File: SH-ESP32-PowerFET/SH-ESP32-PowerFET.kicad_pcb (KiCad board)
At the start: 4 copper layers, 83 x 55.5 mm, 75 parts, among them J101 DBT50G-9.5-4P, J102 DBT50G-9.5-2P, J103 GPIO, J104 Qwiic, J105 MPDI, J106 Conn_01x04, J301 VIN_GND1, Q301 IRF5210STRLPBF, Q302 IRF5210STRLPBF, Q303 IRF5210STRLPBF, Q304 IRF5210STRLPBF, U101 ATtiny1614-SSNR, U301 EL3H7(C)(TA)-G, U302 EL3H7(C)(TA)-G, U303 EL3H7(C)(TA)-G, U304 INA226AIDGSR, U305 INA226AIDGSR, U306 INA226AIDGSR, U307 EL3H7(C)(TA)-G, U308 INA226AIDGSR, U701 RCLAMP0524P-N

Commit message: Updated Shunt Part number
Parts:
- R315: value 0.002ohm /3W -> 0.002ohm/3W

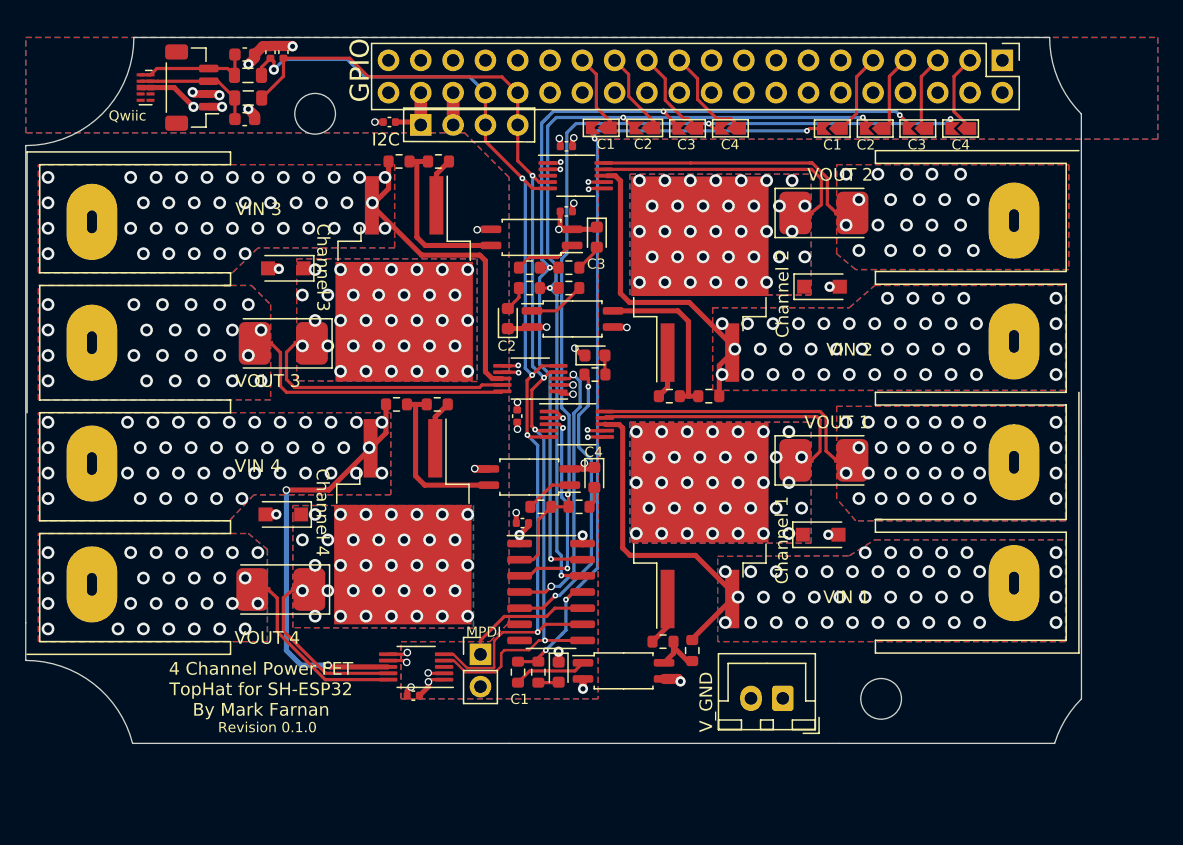
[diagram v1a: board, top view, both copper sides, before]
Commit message: Major Refactor - Based on new requirments from Karl and feedback. - Made from latest blank with more PCB area, and new interconnect positions for I2C,  GPIO etc - Removed opto couplers - I2C now isolated at board input - Provision for Switched inputs and LED outputs - PSU onboard. - I2C only, removed reliance on GPIO header - Can be used as SH-ESP32 HAT,  or as standalone / daisy chained board on DIN rail etc.
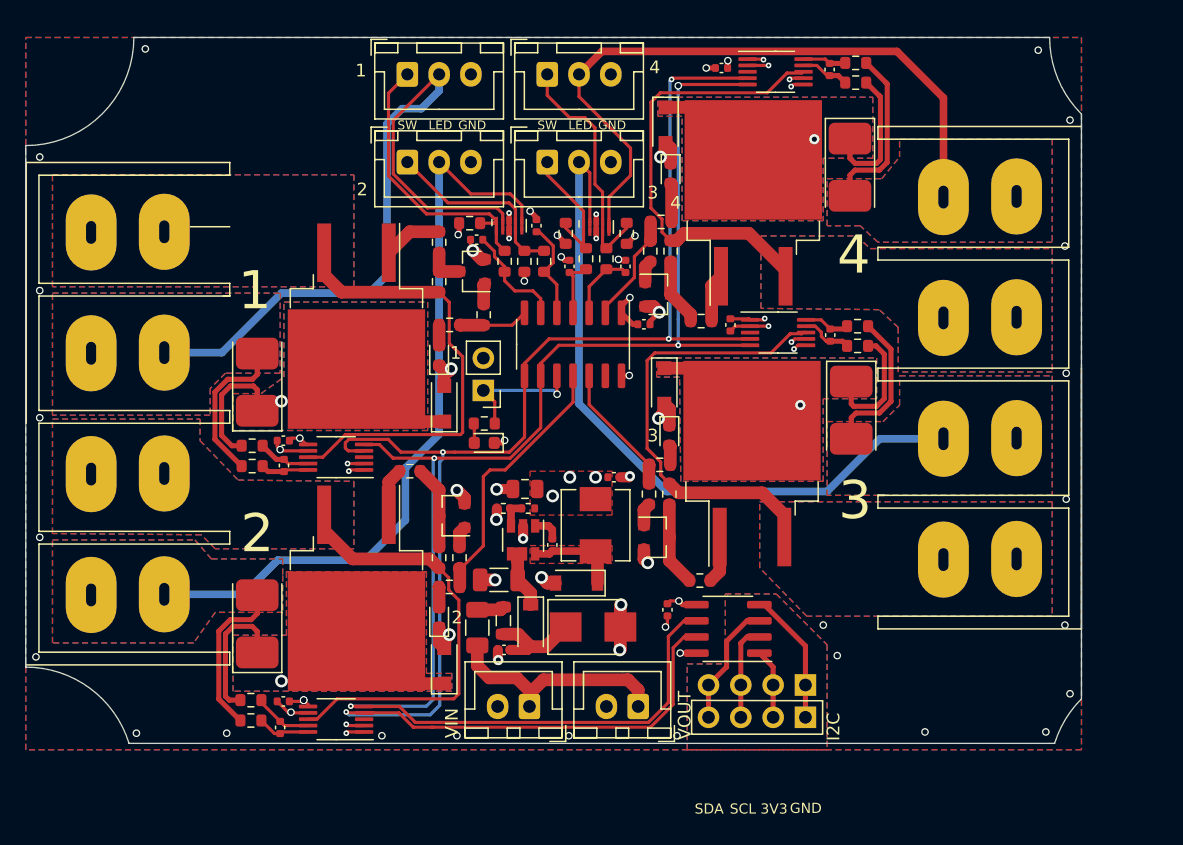
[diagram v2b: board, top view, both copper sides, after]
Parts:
- removed C105, C106: 33pF, Capacitor_SMD:C_0402_1005Metric
- removed D303, D307: BLUE LED, LED_SMD:LED_0603_1608Metric
- removed D304, D305, D306, D308: SM4007PL, Diode_SMD:D_SOD-123F
- removed FB102, FB103: GZ2012D101TF, Inductor_SMD:L_0805_2012Metric
- removed J103: GPIO, Connector_PinHeader_2.54mm:PinHeader_2x20_P2.54mm_Vertical
- removed J104: Qwiic, Connector_JST:JST_SH_BM04B-SRSS-TB_1x04-1MP_P1.00mm_Vertical
- removed J301: VIN_GND1, Connector_JST:JST_XH_B2B-XH-A_1x02_P2.50mm_Vertical
- removed JP101, JP102, JP103, JP104, JP105, JP106, JP107, JP108: Solder Jumper, yacht_hardware:SolderJumper-2_P1.3mm_Open_TrianglePad_Narrow
- removed LOGO_CC: LOGO, SH-ESP32:cc-by-sa_silkscreen
- removed OSHW: OSHW-Logo2_14.6x12mm_SilkScreen, Symbol:OSHW-Logo2_14.6x12mm_SilkScreen
- removed Q303, Q304: IRF5210STRLPBF, Package_TO_SOT_SMD:TO-263-2
- removed R308, R309, R318: 10k, Resistor_SMD:R_0603_1608Metric
- removed R310, R311, R312, R319: 1k, Resistor_SMD:R_0603_1608Metric
- removed R313, R314, R315, R320: 0.002ohm/3W, yacht_hardware:D_2512_Shunt
- removed R316: 2k, Resistor_SMD:R_0603_1608Metric
- removed R317: 220R, Resistor_SMD:R_0603_1608Metric
- removed U302, U303, U307: EL3H7(C)(TA)-G, Package_SO:SOP-4_4.4x2.6mm_P1.27mm
- removed U304, U305, U306, U308: INA226AIDGSR, Package_SO:VSSOP-10_3x3mm_P0.5mm
- added C101: 1nf, Capacitor_SMD:C_0402_1005Metric, F.Cu at (124.5, 72.9)
- added C104: 1nf, Capacitor_SMD:C_0402_1005Metric, F.Cu at (136.2, 75.0)
- added C301: 100nF, Capacitor_SMD:C_0402_1005Metric, F.Cu at (109.3, 90.7)
- added C401: 100nF, Capacitor_SMD:C_0402_1005Metric, F.Cu at (109.0, 111.2)
- added C501: 100nF, Capacitor_SMD:C_0402_1005Metric, F.Cu at (152.2, 80.4)
- added C601: 100nF, Capacitor_SMD:C_0402_1005Metric, F.Cu at (152.2, 59.5)
- added C701: 10uF/50V, Capacitor_SMD:C_1206_3216Metric, F.Cu at (126.2, 99.7)
- added C702: 10nF/50V, Capacitor_SMD:C_0402_1005Metric, F.Cu at (126.6, 105.2)
- added C703: 100nF, Capacitor_SMD:C_0402_1005Metric, F.Cu at (130.4, 96.9)
- added C704: 22uF/6.3V, Capacitor_SMD:C_0805_2012Metric, F.Cu at (128.2, 92.5)
- added C705: 10nF/50V, Capacitor_SMD:C_0402_1005Metric, F.Cu at (135.2, 91.6)
- added D401: BLUE LED, LED_SMD:LED_0603_1608Metric, F.Cu at (121.5, 102.6)
- added D402: SM4007PL, Diode_SMD:D_SOD-123F, F.Cu at (121.9, 106.4)
- added D501: BLUE LED, LED_SMD:LED_0603_1608Metric, F.Cu at (139.6, 88.3)
- added D502: SM4007PL, Diode_SMD:D_SOD-123F, F.Cu at (139.2, 84.4)
- added D601: BLUE LED, LED_SMD:LED_0603_1608Metric, F.Cu at (139.7, 67.7)
- added D602: SM4007PL, Diode_SMD:D_SOD-123F, F.Cu at (139.3, 63.9)
- added D701: SMBJ33CA, Diode_SMD:D_SMB, F.Cu at (133.6, 103.3)
- added D702: B5819W, Diode_SMD:D_SOD-123, F.Cu at (132.3, 99.9)
- added D703: B5819W, Diode_SMD:D_SOD-123, F.Cu at (128.7, 103.2)
- added F701: FSMD012-1206-R, Fuse:Fuse_1206_3216Metric, F.Cu at (124.5, 103.4)
- added FB701: GZ2012D601TF, Inductor_SMD:L_0805_2012Metric, F.Cu at (126.5, 102.8)
- added G***: LOGO, SH-ESP32:Hatlabs-logo-15mm, B.Cu at (78.8, 85.4)
- added G***: LOGO, SH-ESP32:cc-by-sa-10mm, B.Cu at (82.5, 77.9)
- added J107: Switch, Connector_JST:JST_XH_B3B-XH-A_1x03_P2.50mm_Vertical, F.Cu at (119.0, 59.9)
- added J108: Switch, Connector_JST:JST_XH_B3B-XH-A_1x03_P2.50mm_Vertical, F.Cu at (119.0, 66.8)
- added J109: I2C, yacht_hardware:PinHeader_1x04_P2.54mm_Vertical-ShrunkCY, F.Cu at (150.3, 110.5)
- added J110: Switch, Connector_JST:JST_XH_B3B-XH-A_1x03_P2.50mm_Vertical, F.Cu at (130.0, 66.8)
- added J111: Switch, Connector_JST:JST_XH_B3B-XH-A_1x03_P2.50mm_Vertical, F.Cu at (130.0, 59.9)
- added J701: VIN, Connector_JST:JST_XH_B2B-XH-A_1x02_P2.50mm_Vertical, F.Cu at (128.6, 109.6)
- added J702: VOUT, Connector_JST:JST_XH_B2B-XH-A_1x02_P2.50mm_Vertical, F.Cu at (137.2, 109.6)
- added L701: MWSA0503S-100MT, Inductor_SMD:L_Sunlord_MWSA0518_5.4x5.2mm, F.Cu at (133.8, 95.3)
- added Q401: IRLML0030, Package_TO_SOT_SMD:SOT-23, F.Cu at (122.5, 94.6)
- added Q402: IRF5210STRLPBF, Package_TO_SOT_SMD:TO-263-2, F.Cu at (115.0, 100.3)
- added Q501: IRLML0030, Package_TO_SOT_SMD:SOT-23, F.Cu at (138.6, 96.3)
- added Q502: IRF5210STRLPBF, Package_TO_SOT_SMD:TO-263-2, F.Cu at (146.1, 90.5)
- added Q601: IRLML0030, Package_TO_SOT_SMD:SOT-23, F.Cu at (138.7, 77.2)
- added Q602: IRF5210STRLPBF, Package_TO_SOT_SMD:TO-263-2, F.Cu at (146.2, 70.0)
- added R102: 10k, Resistor_SMD:R_0603_1608Metric, F.Cu at (123.9, 71.6)
- added R103: 10k, Resistor_SMD:R_0603_1608Metric, F.Cu at (128.2, 74.6)
- added R104: 10k, Resistor_SMD:R_0603_1608Metric, F.Cu at (131.4, 72.4)
- added R105: 10k, Resistor_SMD:R_0603_1608Metric, F.Cu at (136.2, 72.4)
- added R106: 2k, Resistor_SMD:R_0603_1608Metric, F.Cu at (126.7, 74.6)
- added R107: 2k, Resistor_SMD:R_0603_1608Metric, F.Cu at (129.8, 74.6)
- added R108: 2k, Resistor_SMD:R_0603_1608Metric, F.Cu at (133.1, 74.4)
- added R109: 2k, Resistor_SMD:R_0603_1608Metric, F.Cu at (134.7, 74.4)
- added R401: 2k, Resistor_SMD:R_0603_1608Metric, F.Cu at (122.3, 100.2)
- added R402: 220R, Resistor_SMD:R_0603_1608Metric, F.Cu at (123.1, 97.9)
- added R403: 10k, Resistor_SMD:R_0603_1608Metric, F.Cu at (121.5, 97.9)
- added R404: 1k, Resistor_SMD:R_0603_1608Metric, F.Cu at (119.2, 91.1)
- added R405: 0.002ohm/3W, yacht_hardware:D_2512_Shunt, F.Cu at (107.2, 103.1)
- added R406: 10R, Resistor_SMD:R_0603_1608Metric, F.Cu at (106.7, 109.1)
- added R407: 10R, Resistor_SMD:R_0603_1608Metric, F.Cu at (106.7, 110.7)
- added R501: 2k, Resistor_SMD:R_0603_1608Metric, F.Cu at (138.8, 90.6)
- added R502: 220R, Resistor_SMD:R_0603_1608Metric, F.Cu at (138.0, 92.9)
- added R503: 10k, Resistor_SMD:R_0603_1608Metric, F.Cu at (139.6, 92.9)
- added R504: 1k, Resistor_SMD:R_0603_1608Metric, F.Cu at (142.0, 99.7)
- added R505: 0.002ohm/3W, yacht_hardware:D_2512_Shunt, F.Cu at (153.9, 86.3)
- added R506: 10R, Resistor_SMD:R_0603_1608Metric, F.Cu at (154.4, 81.2)
- added R507: 10R, Resistor_SMD:R_0603_1608Metric, F.Cu at (154.4, 79.7)
- added R601: 2k, Resistor_SMD:R_0603_1608Metric, F.Cu at (138.9, 71.5)
- added R602: 220R, Resistor_SMD:R_0603_1608Metric, F.Cu at (138.1, 73.8)
- added R603: 10k, Resistor_SMD:R_0603_1608Metric, F.Cu at (139.7, 73.8)
- added R604: 1k, Resistor_SMD:R_0603_1608Metric, F.Cu at (142.1, 79.3)
- added R605: 0.002ohm/3W, yacht_hardware:D_2512_Shunt, F.Cu at (153.8, 67.2)
- added R606: 10R, Resistor_SMD:R_0603_1608Metric, F.Cu at (154.2, 60.5)
- added R607: 10R, Resistor_SMD:R_0603_1608Metric, F.Cu at (154.2, 59.0)
- added R701: 68k, Resistor_SMD:R_0402_1005Metric, F.Cu at (128.5, 94.0)
- added R702: 15k, Resistor_SMD:R_0402_1005Metric, F.Cu at (126.5, 94.0)
- added REF**: OSHW-Logo2_9.8x8mm_SilkScreen, Symbol:OSHW-Logo2_9.8x8mm_SilkScreen, B.Cu at (82.5, 71.4)
- added U102: ISO1540, Package_SO:SOIC-8_3.9x4.9mm_P1.27mm, F.Cu at (144.2, 103.5)
- added U103: RCLAMP0524P-N, Package_DFN_QFN:Diodes_UDFN-10_1.0x2.5mm_P0.5mm, F.Cu at (133.8, 71.9)
- added U401: INA226AIDGSR, Package_SO:VSSOP-10_3x3mm_P0.5mm, F.Cu at (113.4, 110.6)
- added U501: INA226AIDGSR, Package_SO:VSSOP-10_3x3mm_P0.5mm, F.Cu at (148.2, 80.2)
- added U601: INA226AIDGSR, Package_SO:VSSOP-10_3x3mm_P0.5mm, F.Cu at (147.9, 59.7)
- added U702: SY8401, Package_TO_SOT_SMD:SOT-23-6, F.Cu at (128.1, 96.5)
- C102, C103: value 33pF/50V -> 1nf; footprint Capacitor_SMD:C_0603_1608Metric -> Capacitor_SMD:C_0402_1005Metric
- D302: value BLUE LED -> SM4007PL; footprint LED_SMD:LED_0603_1608Metric -> Diode_SMD:D_SOD-123F
- H201, H202: footprint SH-ESP32:MountingHole_3.2mm_M3_Unplated -> yacht_hardware:MountingSlot_3.2mm_M3_Unplated
- J106: value Conn_01x04 -> I2C; moved to B.Cu
- Q301: value IRF5210STRLPBF -> IRLML0030; footprint Package_TO_SOT_SMD:TO-263-2 -> Package_TO_SOT_SMD:SOT-23
- R302: value 2k -> 220R
- R303: value 2k -> 10k
- R304: value 220R -> 1k
- R305: value 220R -> 0.002ohm/3W; footprint Resistor_SMD:R_0603_1608Metric -> yacht_hardware:D_2512_Shunt
- R306: value 220R -> 10R
- R307: value 10k -> 10R
- U301: value EL3H7(C)(TA)-G -> INA226AIDGSR; footprint Package_SO:SOP-4_4.4x2.6mm_P1.27mm -> Package_SO:VSSOP-10_3x3mm_P0.5mm
- moved J101 69.3 mm to (97.0, 76.8), turned to 270 degrees
- moved J102 69.2 mm to (164.0, 93.5), turned to 90 degrees
- moved J106 53.4 mm to (150.3, 107.9)
- moved C206 44.1 mm to (139.4, 102.0), turned to 270 degrees
- moved R303 31.7 mm to (121.5, 76.2), turned to 90 degrees
- moved U701 30.6 mm to (127.0, 71.8), turned to 90 degrees
- moved C103 30.5 mm to (131.8, 75.0), turned to 90 degrees
- moved R306 27.5 mm to (106.8, 89.1), turned to 0 degrees
- moved Q302 27.3 mm to (115.0, 79.7), turned to 270 degrees
- moved R307 26.6 mm to (106.8, 90.7), turned to 180 degrees
- moved R305 25.6 mm to (107.2, 84.1), turned to 90 degrees
- moved C102 24.4 mm to (129.2, 71.8), turned to 90 degrees
- moved U301 23.1 mm to (113.4, 90.0)
- moved J105 20.8 mm to (125.0, 84.8), turned to 180 degrees
- moved C201 19.9 mm to (109.2, 88.7)
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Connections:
- C102 pad 1: /SDA_CONN -> /SWITCH_02
- C103 pad 1: /SCL_CONN -> /SWITCH_03
- D302 pad 1: GND -> /FET01/VOUT
- D302 pad 2: Net-(D302-Pad2) -> GND
- J101 pad 1: VIN_01 -> /DRVPWR_01
- J101 pad 2: VOUT_01 -> /DRVOUT_01
- J101 pad 3: VIN_02 -> /DRVPWR_02
- J101 pad 4: VOUT_02 -> /DRVOUT_02
- J102 pad 1: VIN_03 -> /DRVPWR_03
- J102 pad 2: VOUT_03 -> /DRVOUT_03
- J102 pad 3: VIN_04 -> /DRVPWR_04
- J102 pad 4: VOUT_04 -> /DRVOUT_04
- J106 pad 1: GND -> GNDA
- J106 pad 2: +3V3 -> /VCC_CONN_3V3
- J106 pad 3: SCL -> /SDA_CONN
- J106 pad 4: SDA -> /SCL_CONN
- Q301 pad 2: /FET/VOUT3 -> GND
- Q301 pad 3: VIN_03 -> Net-(Q301-Pad3)
- Q302 pad 2: /FET/VOUT2 -> /FET01/VOUT
- Q302 pad 3: VIN_02 -> /DRVPWR_01
- R101 pad 1: Net-(R101-Pad1) -> Net-(J105-Pad1)
- R301 pad 1: FETOUT_03 -> /FETDRIVE_01
- R302 pad 1: FETOUT_02 -> Net-(Q301-Pad1)
- R302 pad 2: Net-(D302-Pad2) -> /FETDRIVE_01
- R303 pad 1: FETOUT_01 -> /DRVPWR_01
- R303 pad 2: Net-(D303-Pad2) -> Net-(Q301-Pad3)
- R304 pad 1: Net-(R304-Pad1) -> Net-(Q302-Pad1)
- R304 pad 2: FETOUT_03 -> Net-(Q301-Pad3)
- R305 pad 1: Net-(R305-Pad1) -> /FET01/VOUT
- R305 pad 2: FETOUT_02 -> /FET01/VOUT
- R306 pad 1: Net-(R306-Pad1) -> /FET01/VOUT
- R306 pad 2: FETOUT_01 -> Net-(C301-Pad1)
- R307 pad 1: VIN_03 -> Net-(C301-Pad2)
- R307 pad 2: Net-(R307-Pad2) -> /DRVOUT_01
- U101 pad 11: FETOUT_01 -> /FETDRIVE_02
- U101 pad 12: FETOUT_02 -> /FETDRIVE_03
- U101 pad 13: FETOUT_03 -> (no net)
- U101 pad 2: FETOUT_04 -> /FETDRIVE_04
- U101 pad 3: ALERT1 -> /SWITCH_04
- U101 pad 4: ALERT4 -> /SWITCH_03
- U101 pad 5: Net-(R101-Pad1) -> /SWITCH_02
- U101 pad 6: (no net) -> /SWITCH_01
- U101 pad 7: (no net) -> /FETDRIVE_01
- U101 pad 8: SDA -> /SDA
- U101 pad 9: SCL -> /SCL
- U301 pad 1: Net-(R304-Pad1) -> GND
- U301 pad 3: GND1 -> (no net)
- U301 pad 4: Net-(R307-Pad2) -> /SDA
- U701 pad 1: /SCL_CONN -> Net-(J107-Pad1)
- U701 pad 10: /SCL_CONN -> Net-(J107-Pad1)
- U701 pad 2: /SDA_CONN -> /DRVOUT_01
- U701 pad 4: (no net) -> Net-(J108-Pad1)
- U701 pad 5: (no net) -> /DRVOUT_02
- U701 pad 6: (no net) -> /DRVOUT_02
- U701 pad 7: (no net) -> Net-(J108-Pad1)
- U701 pad 9: /SDA_CONN -> /DRVOUT_01
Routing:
- net /SDA: track 0.00 -> 130.7 mm, vias 0 -> 4
- net /SCL: track 0.00 -> 123.2 mm, vias 0 -> 4
- net SDA: track 86.8 -> 0.00 mm, vias 4 -> 0
- net SCL: track 85.5 -> 0.00 mm, vias 5 -> 0
- net /DRVOUT_02: track 0.00 -> 73.3 mm
- net FETOUT_03: track 71.7 -> 0.00 mm, vias 4 -> 0
- net /DRVOUT_01: track 0.00 -> 71.2 mm
- net /DRVOUT_03: track 0.00 -> 70.0 mm
- net FETOUT_04: track 69.6 -> 0.00 mm, vias 3 -> 0
- net /DRVOUT_04: track 0.00 -> 67.7 mm
- net FETOUT_02: track 66.7 -> 0.00 mm, vias 4 -> 0
- net FETOUT_01: track 66.0 -> 0.00 mm, vias 4 -> 0
- net /DRVPWR_01: track 0.00 -> 36.1 mm
- net /DRVPWR_03: track 0.00 -> 35.6 mm
- net /DRVPWR_04: track 0.00 -> 35.5 mm
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- added copper zone on F.Cu, net +3V3
- added copper zone on B.Cu, net /DRVOUT_01
- added copper zone on F.Cu, net /DRVOUT_01
- added copper zone on B.Cu, net /DRVOUT_02
- added copper zone on F.Cu, net /DRVOUT_02
- added copper zone on B.Cu, net /DRVOUT_03
- added copper zone on F.Cu, net /DRVOUT_03
- added copper zone on B.Cu, net /DRVOUT_04
- added copper zone on F.Cu, net /DRVOUT_04
- added copper zone on B.Cu, net /DRVPWR_01
- added copper zone on F.Cu, net /DRVPWR_01
- added copper zone on B.Cu, net /DRVPWR_02
- added copper zone on F.Cu, net /DRVPWR_02
- added copper zone on B.Cu, net /DRVPWR_03
- added copper zone on F.Cu, net /DRVPWR_03
- added copper zone on B.Cu, net /DRVPWR_04
- added copper zone on F.Cu, net /DRVPWR_04
- added copper zone on B.Cu, net /FET01/VOUT
- added copper zone on F.Cu, net /FET01/VOUT
- added copper zone on B.Cu, net /FET02/VOUT
- added copper zone on F.Cu, net /FET02/VOUT
- added copper zone on B.Cu, net /FET03/VOUT
- added copper zone on F.Cu, net /FET03/VOUT
- added copper zone on B.Cu, net /FET04/VOUT
- added copper zone on F.Cu, net /FET04/VOUT
- added copper zone on F.Cu, net /Power-Input/SW
- added copper zone on B.Cu, net GNDA
- added copper zone on F.Cu, net GNDA
- added copper zone on In1.Cu, net GNDA
- added copper zone on In2.Cu, net GNDA
- removed copper zone on B.Cu, net /FET/VOUT1
- removed copper zone on F.Cu, net /FET/VOUT1
- removed copper zone on B.Cu, net /FET/VOUT2
- removed copper zone on F.Cu, net /FET/VOUT2
- removed copper zone on B.Cu, net /FET/VOUT3
- removed copper zone on F.Cu, net /FET/VOUT3
- removed copper zone on B.Cu, net /FET/VOUT4
- removed copper zone on F.Cu, net /FET/VOUT4
- removed copper zone on In1.Cu, net GND1
- removed copper zone on B.Cu, net VIN_01
- removed copper zone on F.Cu, net VIN_01
- removed copper zone on B.Cu, net VIN_02
- removed copper zone on F.Cu, net VIN_02
- removed copper zone on B.Cu, net VIN_03
- removed copper zone on F.Cu, net VIN_03
- removed copper zone on B.Cu, net VIN_04
- removed copper zone on F.Cu, net VIN_04
- removed copper zone on B.Cu, net VOUT_01
- removed copper zone on F.Cu, net VOUT_01
- removed copper zone on B.Cu, net VOUT_02
- removed copper zone on F.Cu, net VOUT_02
- removed copper zone on B.Cu, net VOUT_03
- removed copper zone on F.Cu, net VOUT_03
- removed copper zone on B.Cu, net VOUT_04
- removed copper zone on F.Cu, net VOUT_04
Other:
- outline, holes or cut-outs redrawn
- board text added: "1"
- board text added: "2"
- board text added: "3"
- board text added: "4"
- board text added: "GND & 3.3V"
- board text added: "LED"
- board text added: "Revision 0.3.0"
- board text added: "SW"
- board text added: "Sailor Hat with ESP32"
- board text added: "VIN"
- board text added: "VOUT"
- board text added: "https://github.com/hatlabs/SH-ESP32-hardware/"
- board text removed: "4 Channel Power FET TopHat for SH-ESP32 By Mark Farnan"
- board text removed: "C1"
- board text removed: "C2"
- board text removed: "C3"
- board text removed: "C4"
- board text removed: "Channel 1"
- board text removed: "Channel 2"
- board text removed: "Channel 3"
- board text removed: "Channel 4"
- board text removed: "GPIO"
- board text removed: "JLCJLCJLCJLC"
- board text removed: "MPDI"
- board text removed: "Qwiic"
- board text removed: "Revision 0.1.0"
- board text removed: "VIN 1"
- board text removed: "VIN 2"
- board text removed: "VIN 3"
- board text removed: "VIN 4"
- board text removed: "VOUT 1"
- board text removed: "VOUT 2"
- board text removed: "VOUT 3"
- board text removed: "VOUT 4"
- board text removed: "V_GND"
- board text removed: "htts://github.com/markfarnan"

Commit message: Fix I2C Address selection to support up to 4 boards - Add pullups to I2C
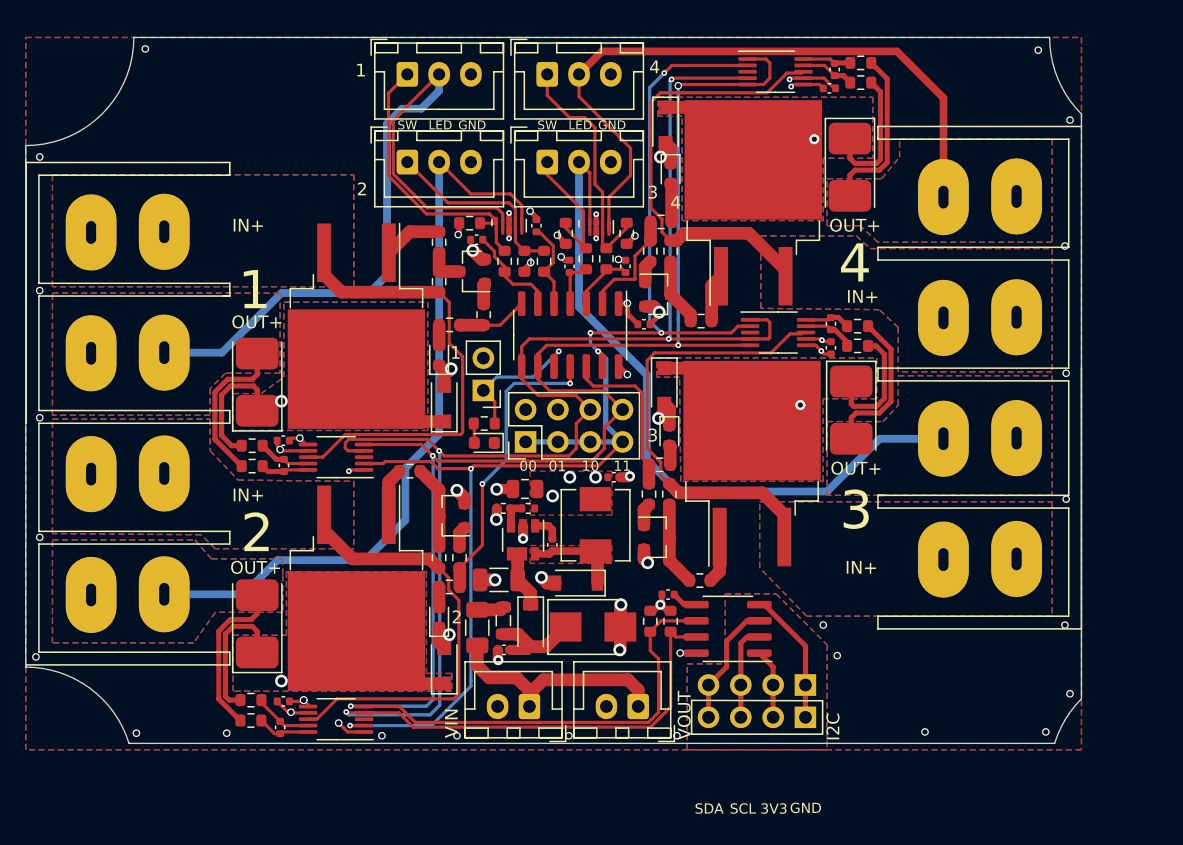
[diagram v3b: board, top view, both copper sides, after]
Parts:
- added J103: AddressSelect, yacht_hardware:PinHeader_2x04_P2.54mm_Vertical_ReducedCY_Jumper, F.Cu at (128.3, 88.8)
- added R110: 10k, Resistor_SMD:R_0603_1608Metric, F.Cu at (139.7, 102.9)
- added R111: 10k, Resistor_SMD:R_0603_1608Metric, F.Cu at (138.1, 102.9)
- moved C202 8.63 mm to (152.2, 61.0), turned to 180 degrees
- moved C203 8.10 mm to (152.3, 81.4)
- moved C206 1.20 mm to (139.5, 100.8), turned to 180 degrees
- moved C501 0.90 mm to (152.3, 79.5)
- moved U101 0.76 mm to (131.8, 80.4)
- moved C601 0.40 mm to (152.6, 59.5)
- moved R606 0.40 mm to (154.7, 60.5)
- moved R607 0.40 mm to (154.7, 59.0)
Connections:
- U101 pad 13: (no net) -> /ASEL
- U301 pad 2: GND -> /ASEL
- U401 pad 2: GND -> /ASEL
- U501 pad 1: GND -> /SDA
- U501 pad 2: +3V3 -> /ASEL
- U601 pad 1: +3V3 -> /SCL
- U601 pad 2: +3V3 -> /ASEL
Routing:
- net /ASEL: track 0.00 -> 109.9 mm, vias 0 -> 6
- net /SCL: track 123.2 -> 143.9 mm
- net /SDA: track 130.7 -> 147.8 mm
- net GND: track 55.2 -> 51.6 mm, vias 59 -> 53
- net /FETDRIVE_03: track 10.4 -> 13.2 mm
- net /FETDRIVE_02: track 21.1 -> 23.5 mm, vias 0 -> 2
- net +3V3: track 23.1 -> 21.8 mm, vias 20 -> 16
- net Net-(J105-Pad1): track 10.4 -> 11.5 mm
- net /SWITCH_01: track 8.47 -> 7.64 mm
- net /SWITCH_03: track 4.69 -> 3.87 mm
- net /SWITCH_02: track 7.77 -> 6.95 mm
- net /SWITCH_04: track 5.59 -> 4.96 mm
- net /DRVOUT_03: track 70.0 -> 69.5 mm
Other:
- board text added: "00"
- board text added: "01"
- board text added: "10"
- board text added: "11"
- board text added: "Board Select"
- board text added: "IN+"
- board text added: "OUT+"

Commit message: Tidy Planes on back side - Change I2C header to Socket for HAT connection to SH_ESP32
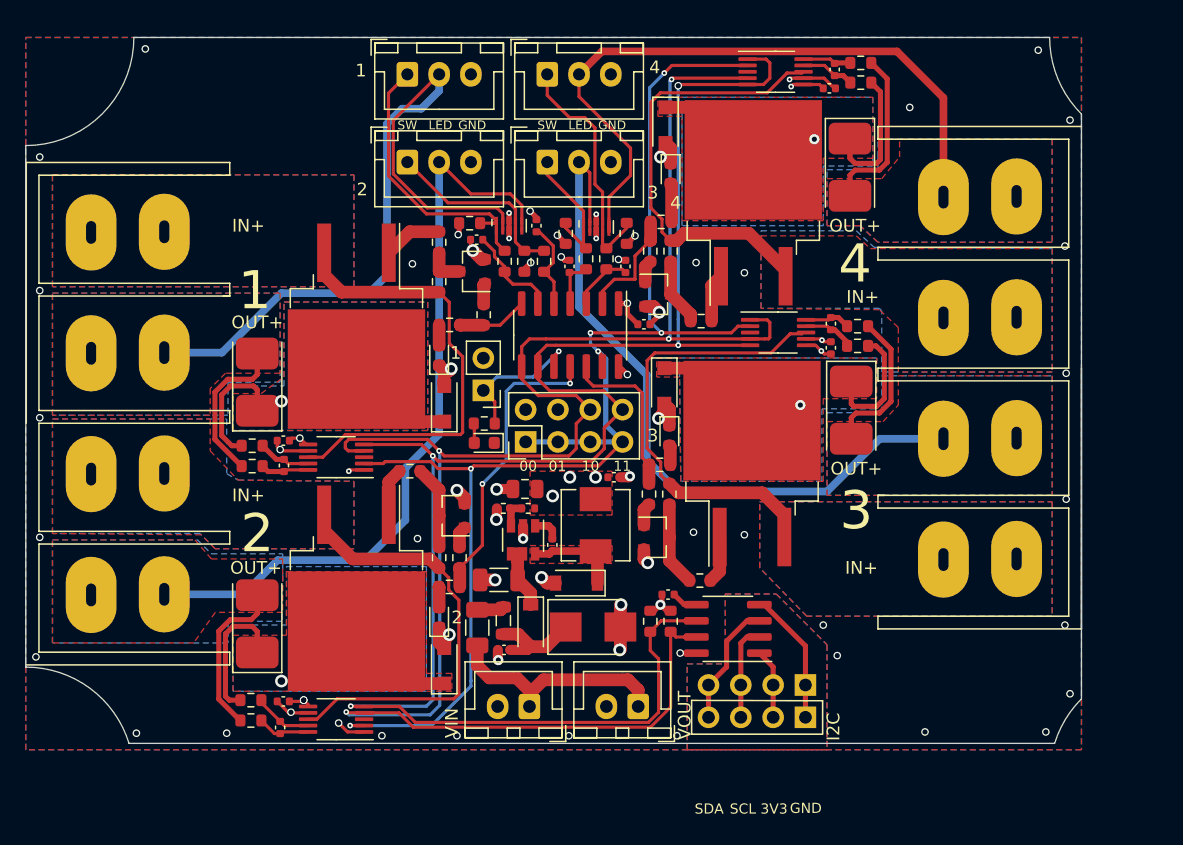
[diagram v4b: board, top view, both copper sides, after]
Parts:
- removed the G*** at (78.8, 85.4)
- J106: footprint yacht_hardware:PinHeader_1x04_P2.54mm_Vertical-ShrunkCY -> Connector_PinSocket_2.54mm:PinSocket_1x04_P2.54mm_Vertical
- moved REF** 48.0 mm to (124.1, 95.5)
- moved G*** 47.6 mm to (124.1, 101.1)
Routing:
- net GND: vias 53 -> 60
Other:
- board text added: "By Mark Farnan"
- board text added: "FET Switch for SH_ESP32"
- board text added: "https://github.com/markfarnan"
- board text removed: "Sailor Hat with ESP32"
- board text removed: "https://github.com/hatlabs/SH-ESP32-hardware/"

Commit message: Change Buck PSU for a LDO Regulator - Allowed input from VIN-Protected from SH-ESP32 when in HAT mode.  (2 pin socket).   - Saves wiring and sockets etc. - Shoved ScrewTerminal to permit VIN-Prot header pads. - Added some Nets (Mairas)
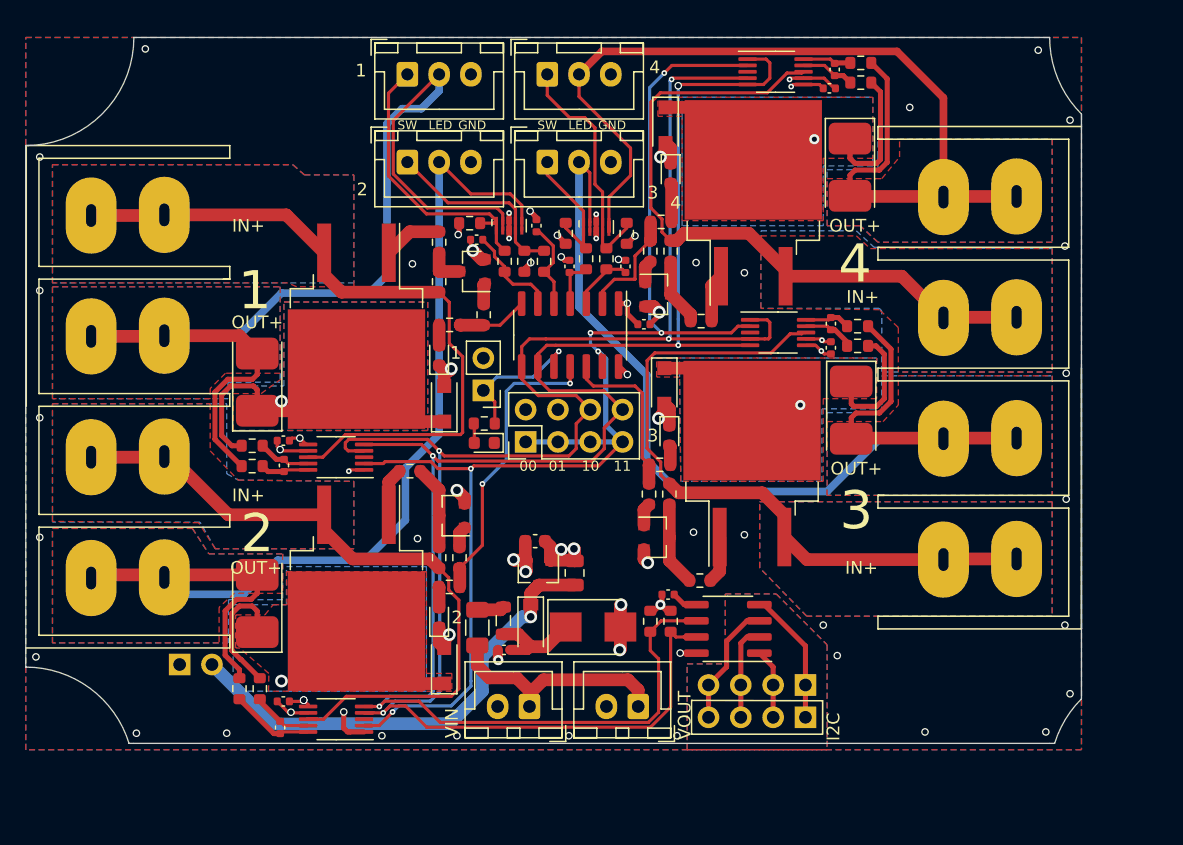
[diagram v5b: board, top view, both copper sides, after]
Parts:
- removed C704: 22uF/6.3V, Capacitor_SMD:C_0805_2012Metric
- removed C705: 10nF/50V, Capacitor_SMD:C_0402_1005Metric
- removed D702: B5819W, Diode_SMD:D_SOD-123
- removed L701: MWSA0503S-100MT, Inductor_SMD:L_Sunlord_MWSA0518_5.4x5.2mm
- removed R701: 68k, Resistor_SMD:R_0402_1005Metric
- removed R702: 15k, Resistor_SMD:R_0402_1005Metric
- added J703: VOUT, Connector_PinSocket_2.54mm:PinSocket_1x02_P2.54mm_Vertical, B.Cu at (101.1, 106.3)
- C701: value 10uF/50V -> 2.2uF/50V; footprint Capacitor_SMD:C_1206_3216Metric -> Capacitor_SMD:C_0805_2012Metric
- C703: value 100nF -> 2.2uF/16V; footprint Capacitor_SMD:C_0402_1005Metric -> Capacitor_SMD:C_0603_1608Metric
- J105: value MPDI -> UPDI
- U702: value SY8401 -> H7533-H#; footprint Package_TO_SOT_SMD:SOT-23-6 -> Package_TO_SOT_SMD:SOT-23
- moved C701 5.98 mm to (132.2, 99.1), turned to 90 degrees
- moved U702 2.86 mm to (129.3, 99.1)
- moved R407 2.66 mm to (105.8, 108.2), turned to 90 degrees
- moved R405 1.60 mm to (107.2, 101.5)
- moved C703 1.38 mm to (129.1, 96.6), turned to 0 degrees
- moved J101 1.33 mm to (97.0, 75.5)
- moved R406 1.14 mm to (107.4, 108.2), turned to 270 degrees
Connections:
- net Net-(J105-Pad1) renamed /UPDI_LED
- net Net-(J107-Pad1) renamed /SWIN_1
- net Net-(J108-Pad1) renamed /SWIN_2
- net Net-(J110-Pad1) renamed /SWIN_3
- net Net-(J111-Pad1) renamed /SWIN_4
- C703 pad 1: /Power-Input/SW -> +3V3
- C703 pad 2: /Power-Input/BS -> GND
- U702 pad 1: /Power-Input/BS -> GND
- U702 pad 2: GND -> +3V3
- U702 pad 3: /Power-Input/FB -> /Power-Input/Vin_protected
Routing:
- net /Power-Input/Vin_protected: track 5.99 -> 38.1 mm, vias 0 -> 1
- net /DRVPWR_02: track 34.7 -> 56.1 mm
- net /DRVPWR_01: track 36.1 -> 55.7 mm
- net /DRVPWR_04: track 35.5 -> 55.0 mm
- net /DRVPWR_03: track 35.6 -> 54.6 mm
- net /DRVOUT_04: track 67.6 -> 80.7 mm
- net /DRVOUT_01: track 71.2 -> 84.3 mm
- net /DRVOUT_03: track 69.5 -> 82.5 mm
- net /DRVOUT_02: track 73.3 -> 84.0 mm
- net /FET01/VOUT: track 18.6 -> 27.7 mm
- net /Power-Input/SW: track 7.41 -> 0.00 mm
- net /SDA: track 147.8 -> 143.1 mm
- net +3V3: track 21.8 -> 26.0 mm, vias 16 -> 15
- net /SCL: track 143.9 -> 140.4 mm
- net Net-(C401-Pad2): track 4.16 -> 6.57 mm
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- removed copper zone on F.Cu, net +3V3
- removed copper zone on F.Cu, net /Power-Input/SW
